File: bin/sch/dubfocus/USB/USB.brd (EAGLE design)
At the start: 39.8 x 15.5 mm, 3 parts

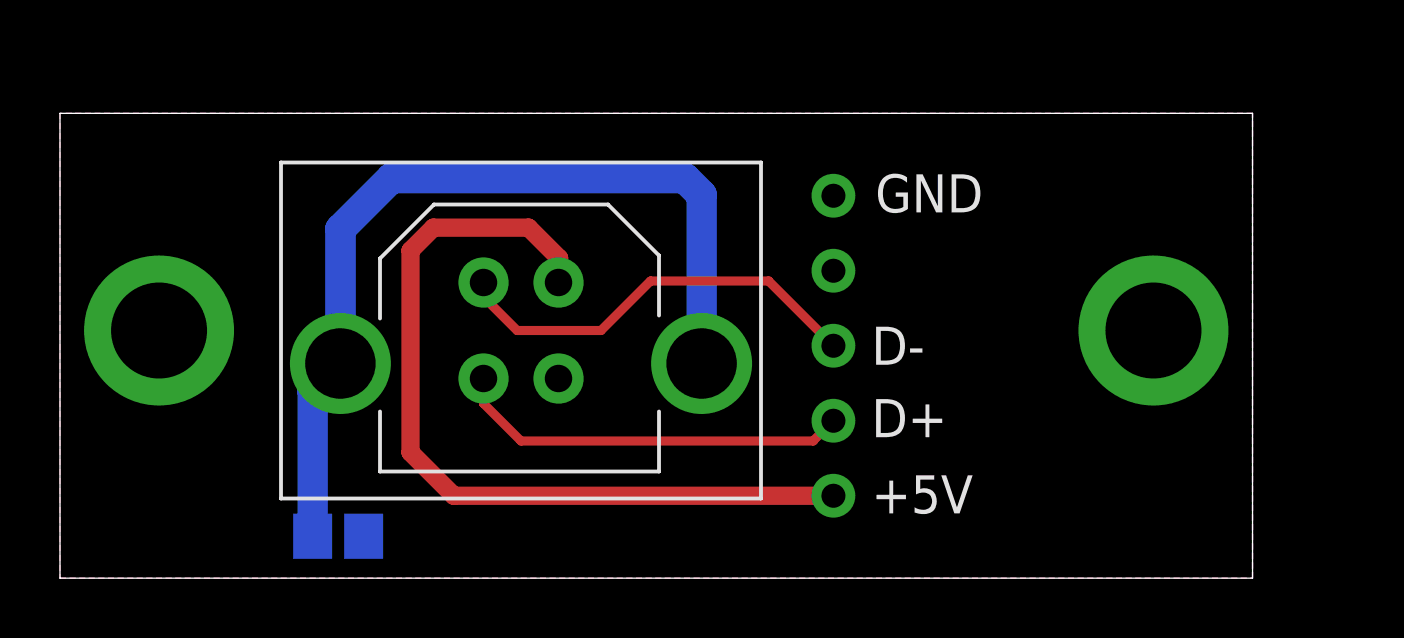
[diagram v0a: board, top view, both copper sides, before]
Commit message: targets: update schematics for dubfocus
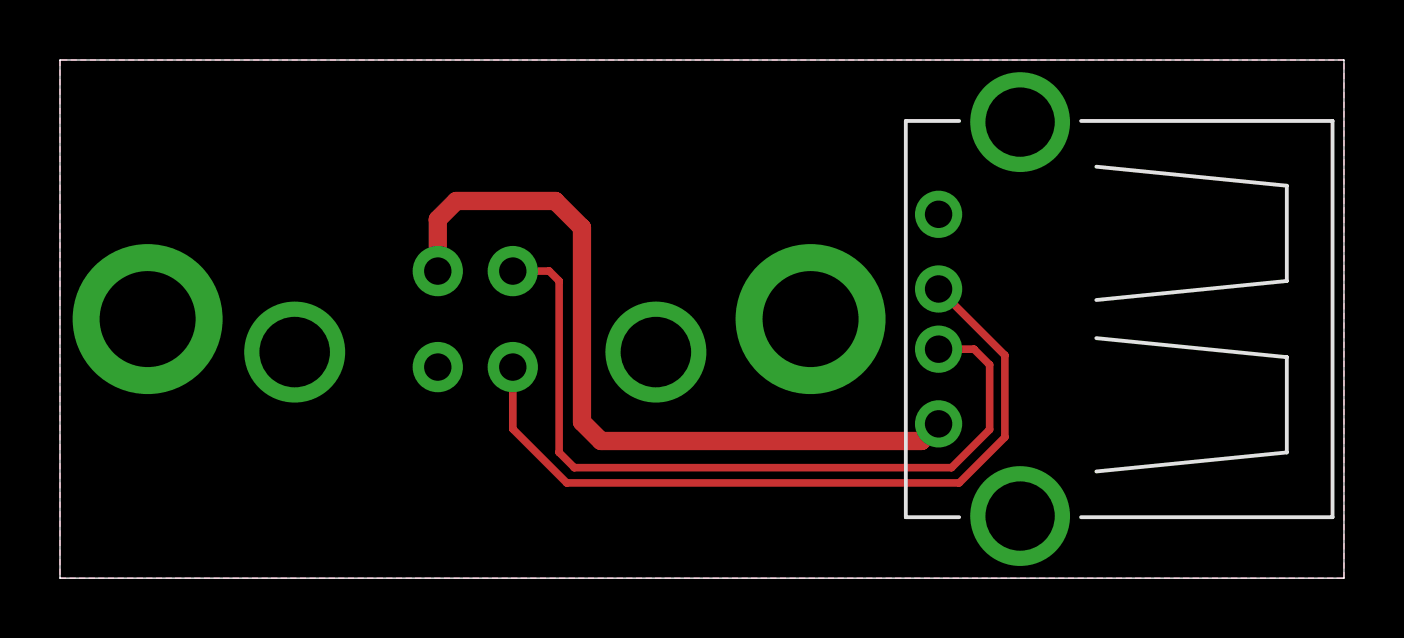
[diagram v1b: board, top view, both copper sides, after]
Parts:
- removed L1: FERRITE_BEAD-BLM21PG221SN1D, igor_lbr:L0805
- CONN1: value USB-V -> USB-B-V
- CONN2: value PINHD-1X05-JST-XH-H -> USB-A-H; device igor_lbr:JST-XH-05P-H -> igor_lbr:USB-A-PTH
- moved CONN2 8.81 mm to (34.5, 8.64), flipped to the top, turned to 180 degrees
- moved CONN1 1.57 mm to (13.8, 8.64), flipped to the bottom
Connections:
- removed net N$1: CONN1.S1, CONN1.S2, L1.1
- net +5V: now also CONN2.VBUS; no longer CONN2.1
- net D+: now also CONN2.D+; no longer CONN2.2
- net D-: now also CONN2.D-; no longer CONN2.3
- net GND: now also CONN1.S1, CONN1.S2, CONN2.GND, CONN2.S1, CONN2.S2; no longer CONN2.5, L1.2
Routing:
- net N$1: track 29.2 -> 0.00 mm
- net D+: track 13.3 -> 25.7 mm
- net D-: track 14.2 -> 26.6 mm
- net +5V: track 27.9 -> 26.0 mm
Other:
- board size 39.8 x 15.5 mm -> 42.8 x 17.3 mm
- board text removed: "+5V"
- board text removed: "D+"
- board text removed: "D-"
- board text removed: "GND"
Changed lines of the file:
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@@
 <board>
 <plain>
-<text x="27.051" y="2.159" size="1.27" layer="25" font="vector" ratio="15">+5V</text>
-<text x="27.051" y="4.699" size="1.27" layer="25" font="vector" ratio="15">D+</text>
-<text x="27.051" y="7.112" size="1.27" layer="25" font="vector" ratio="15">D-</text>
-<text x="27.178" y="12.192" size="1.27" layer="25" font="vector" ratio="15">GND</text>
-<wire x1="39.751" y1="15.494" x2="39.751" y2="0" width="0" layer="20"/>
-<wire x1="39.751" y1="0" x2="0" y2="0" width="0" layer="20"/>
-<wire x1="0" y1="0" x2="0" y2="15.494" width="0" layer="20"/>
-<wire x1="0" y1="15.494" x2="39.751" y2="15.494" width="0" layer="20"/>
+<wire x1="42.799" y1="17.272" x2="42.799" y2="0" width="0" layer="20"/>
+<wire x1="42.799" y1="0" x2="0" y2="0" width="0" layer="20"/>
+<wire x1="0" y1="0" x2="0" y2="17.272" width="0" layer="20"/>
+<wire x1="0" y1="17.272" x2="42.799" y2="17.272" width="0" layer="20"/>
 </plain>
 <attributes>
@@
 </autorouter>
 <elements>
-<element name="CONN1" library="igor_lbr" package="USB-B-PTH-V" value="USB-V" x="15.367" y="8.255" smashed="yes">
-<attribute name="MANUFACTURER" value="CUI Devices" x="15.367" y="8.255" size="1.778" layer="27" display="off"/>
-<attribute name="MPN" value="UJ2-BV-1-TH" x="15.367" y="8.255" size="1.778" layer="27" display="off"/>
+<element name="CONN1" library="igor_lbr" package="USB-B-PTH-V" value="USB-B-V" x="13.843" y="8.636" smashed="yes" rot="MR0">
+<attribute name="MANUFACTURER" value="CUI Devices" x="13.843" y="8.636" size="1.778" layer="28" rot="MR0" display="off"/>
+<attribute name="MPN" value="UJ2-BV-1-TH" x="13.843" y="8.636" size="1.778" layer="28" rot="MR0" display="off"/>
 </element>
-<element name="CONN2" library="igor_lbr" package="JST-XH-05P-H" value="PINHD-1X05-JST-XH-H" x="25.781" y="7.747" smashed="yes" rot="MR90"/>
-<element name="L1" library="igor_lbr" package="L0805" value="FERRITE_BEAD-BLM21PG221SN1D" x="9.271" y="1.397" smashed="yes" rot="MR180">
-<attribute name="MANUFACTURER" value="Murata" x="9.271" y="1.397" size="1.778" layer="28" rot="MR180" display="off"/>
-<attribute name="MPN" value="BLM21PG221SN1D" x="9.271" y="1.397" size="1.778" layer="28" rot="MR180" display="off"/>
-<attribute name="NAME" x="11.43" y="0.381" size="1.27" layer="26" font="vector" ratio="15" rot="MR90"/>
-</element>
+<element name="CONN2" library="igor_lbr" package="USB-A-PTH" value="USB-A-H" x="34.544" y="8.636" smashed="yes" rot="R180"/>
 </elements>
 <signals>
 <signal name="D+">
 <contactref element="CONN1" pad="D+"/>
-<contactref element="CONN2" pad="2"/>
-<wire x1="14.117" y1="6.655" x2="14.117" y2="5.822" width="0.3048" layer="1"/>
-<wire x1="14.117" y1="5.822" x2="15.367" y2="4.572" width="0.3048" layer="1"/>
-<wire x1="15.367" y1="4.572" x2="25.106" y2="4.572" width="0.3048" layer="1"/>
-<wire x1="25.106" y1="4.572" x2="25.781" y2="5.247" width="0.3048" layer="1"/>
+<contactref element="CONN2" pad="D+"/>
+<wire x1="15.093" y1="7.036" x2="15.093" y2="4.973" width="0.254" layer="1"/>
+<wire x1="15.093" y1="4.973" x2="16.891" y2="3.175" width="0.254" layer="1"/>
+<wire x1="16.891" y1="3.175" x2="29.972" y2="3.175" width="0.254" layer="1"/>
+<wire x1="29.972" y1="3.175" x2="31.496" y2="4.699" width="0.254" layer="1"/>
+<wire x1="31.496" y1="4.699" x2="31.496" y2="7.4295" width="0.254" layer="1"/>
+<wire x1="31.496" y1="7.4295" x2="29.2862" y2="9.6393" width="0.254" layer="1"/>
 </signal>
 <signal name="D-">
 <contactref element="CONN1" pad="D-"/>
-<contactref element="CONN2" pad="3"/>
-<wire x1="14.117" y1="9.855" x2="14.117" y2="9.378" width="0.3048" layer="1"/>
-<wire x1="14.117" y1="9.378" x2="15.24" y2="8.255" width="0.3048" layer="1"/>
-<wire x1="15.24" y1="8.255" x2="18.034" y2="8.255" width="0.3048" layer="1"/>
-<wire x1="18.034" y1="8.255" x2="19.685" y2="9.906" width="0.3048" layer="1"/>
-<wire x1="19.685" y1="9.906" x2="23.622" y2="9.906" width="0.3048" layer="1"/>
-<wire x1="23.622" y1="9.906" x2="25.781" y2="7.747" width="0.3048" layer="1"/>
+<contactref element="CONN2" pad="D-"/>
+<wire x1="15.093" y1="10.236" x2="16.307" y2="10.236" width="0.254" layer="1"/>
+<wire x1="16.307" y1="10.236" x2="16.637" y2="9.906" width="0.254" layer="1"/>
+<wire x1="16.637" y1="9.906" x2="16.637" y2="4.191" width="0.254" layer="1"/>
+<wire x1="16.637" y1="4.191" x2="17.145" y2="3.683" width="0.254" layer="1"/>
+<wire x1="17.145" y1="3.683" x2="29.718" y2="3.683" width="0.254" layer="1"/>
+<wire x1="29.718" y1="3.683" x2="30.988" y2="4.953" width="0.254" layer="1"/>
+<wire x1="30.988" y1="4.953" x2="30.988" y2="7.112" width="0.254" layer="1"/>
+<wire x1="29.2862" y1="7.6327" x2="30.4673" y2="7.6327" width="0.254" layer="1"/>
+<wire x1="30.4673" y1="7.6327" x2="30.988" y2="7.112" width="0.254" layer="1"/>
 </signal>
 <signal name="GND">
 <contactref element="CONN1" pad="GND"/>
-<contactref element="L1" pad="2"/>
-<contactref element="CONN2" pad="5"/>
 <polygon width="0.254" layer="1" isolate="0.3048">
-<vertex x="0" y="15.494"/>
+<vertex x="0" y="17.272"/>
 <vertex x="0" y="0"/>
-<vertex x="39.751" y="0"/>
-<vertex x="39.751" y="15.494"/>
+<vertex x="42.799" y="0"/>
+<vertex x="42.799" y="17.272"/>
 </polygon>
 <polygon width="0.254" layer="16" isolate="0.3048">
-<vertex x="0" y="15.494"/>
+<vertex x="0" y="17.272"/>
 <vertex x="0" y="0"/>
-<vertex x="39.751" y="0"/>
-<vertex x="39.751" y="15.494"/>
+<vertex x="42.799" y="0"/>
+<vertex x="42.799" y="17.272"/>
 </polygon>
-<via x="3.302" y="8.255" extent="1-16" drill="3.2" diameter="5"/>
-<via x="36.449" y="8.255" extent="1-16" drill="3.2" diameter="5"/>
+<contactref element="CONN2" pad="GND"/>
+<via x="2.921" y="8.636" extent="1-16" drill="3.2" diameter="5"/>
+<via x="25.019" y="8.636" extent="1-16" drill="3.2" diameter="5"/>
+<contactref element="CONN1" pad="S1"/>
+<contactref element="CONN1" pad="S2"/>
+<contactref element="CONN2" pad="S1"/>
+<contactref element="CONN2" pad="S2"/>
 </signal>
 <signal name="+5V">
 <contactref element="CONN1" pad="VBUS"/>
-<contactref element="CONN2" pad="1"/>
-<wire x1="25.781" y1="2.747" x2="13.128" y2="2.747" width="0.6096" layer="1"/>
-<wire x1="13.128" y1="2.747" x2="11.684" y2="4.191" width="0.6096" layer="1"/>
-<wire x1="11.684" y1="4.191" x2="11.684" y2="10.922" width="0.6096" layer="1"/>
-<wire x1="11.684" y1="10.922" x2="12.446" y2="11.684" width="0.6096" layer="1"/>
-<wire x1="12.446" y1="11.684" x2="15.621" y2="11.684" width="0.6096" layer="1"/>
-<wire x1="15.621" y1="11.684" x2="16.637" y2="10.668" width="0.6096" layer="1"/>
-<wire x1="16.637" y1="10.668" x2="16.637" y2="9.875" width="0.6096" layer="1"/>
-<wire x1="16.637" y1="9.875" x2="16.617" y2="9.855" width="0.6096" layer="1"/>
-</signal>
-<signal name="N$1">
-<contactref element="CONN1" pad="S1"/>
-<contactref element="CONN1" pad="S2"/>
-<contactref element="L1" pad="1"/>
-<wire x1="9.347" y1="7.155" x2="9.347" y2="11.633" width="1.016" layer="16"/>
-<wire x1="9.347" y1="11.633" x2="11.049" y2="13.335" width="1.016" layer="16"/>
-<wire x1="11.049" y1="13.335" x2="20.828" y2="13.335" width="1.016" layer="16"/>
-<wire x1="20.828" y1="13.335" x2="21.387" y2="12.776" width="1.016" layer="16"/>
-<wire x1="21.387" y1="7.155" x2="21.387" y2="12.776" width="1.016" layer="16"/>
-<wire x1="8.421" y1="1.397" x2="8.421" y2="6.229" width="1.016" layer="16"/>
-<wire x1="8.421" y1="6.229" x2="9.347" y2="7.155" width="1.016" layer="16"/>
+<contactref element="CONN2" pad="VBUS"/>
+<wire x1="12.593" y1="10.236" x2="12.593" y2="11.958" width="0.6096" layer="1"/>
+<wire x1="12.593" y1="11.958" x2="13.208" y2="12.573" width="0.6096" layer="1"/>
+<wire x1="13.208" y1="12.573" x2="16.51" y2="12.573" width="0.6096" layer="1"/>
+<wire x1="16.51" y1="12.573" x2="17.399" y2="11.684" width="0.6096" layer="1"/>
+<wire x1="17.399" y1="11.684" x2="17.399" y2="5.207" width="0.6096" layer="1"/>
+<wire x1="17.399" y1="5.207" x2="18.034" y2="4.572" width="0.6096" layer="1"/>
+<wire x1="18.034" y1="4.572" x2="28.7147" y2="4.572" width="0.6096" layer="1"/>
+<wire x1="28.7147" y1="4.572" x2="29.2862" y2="5.1435" width="0.6096" layer="1"/>
+</signal>
+<signal name="VBUS">
 </signal>
 </signals>
